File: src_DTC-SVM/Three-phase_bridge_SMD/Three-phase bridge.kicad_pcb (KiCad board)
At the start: 2 copper layers, 419.1 x 318 mm, 92 parts, among them M1 MCP6022-I/P, M2 MCP6022-I/P, P1 CONN_1, P2 POWER_FUSE, P3 CONN_2, P4 CONN_1, P5 CONN_1, P6 POWER_FUSE

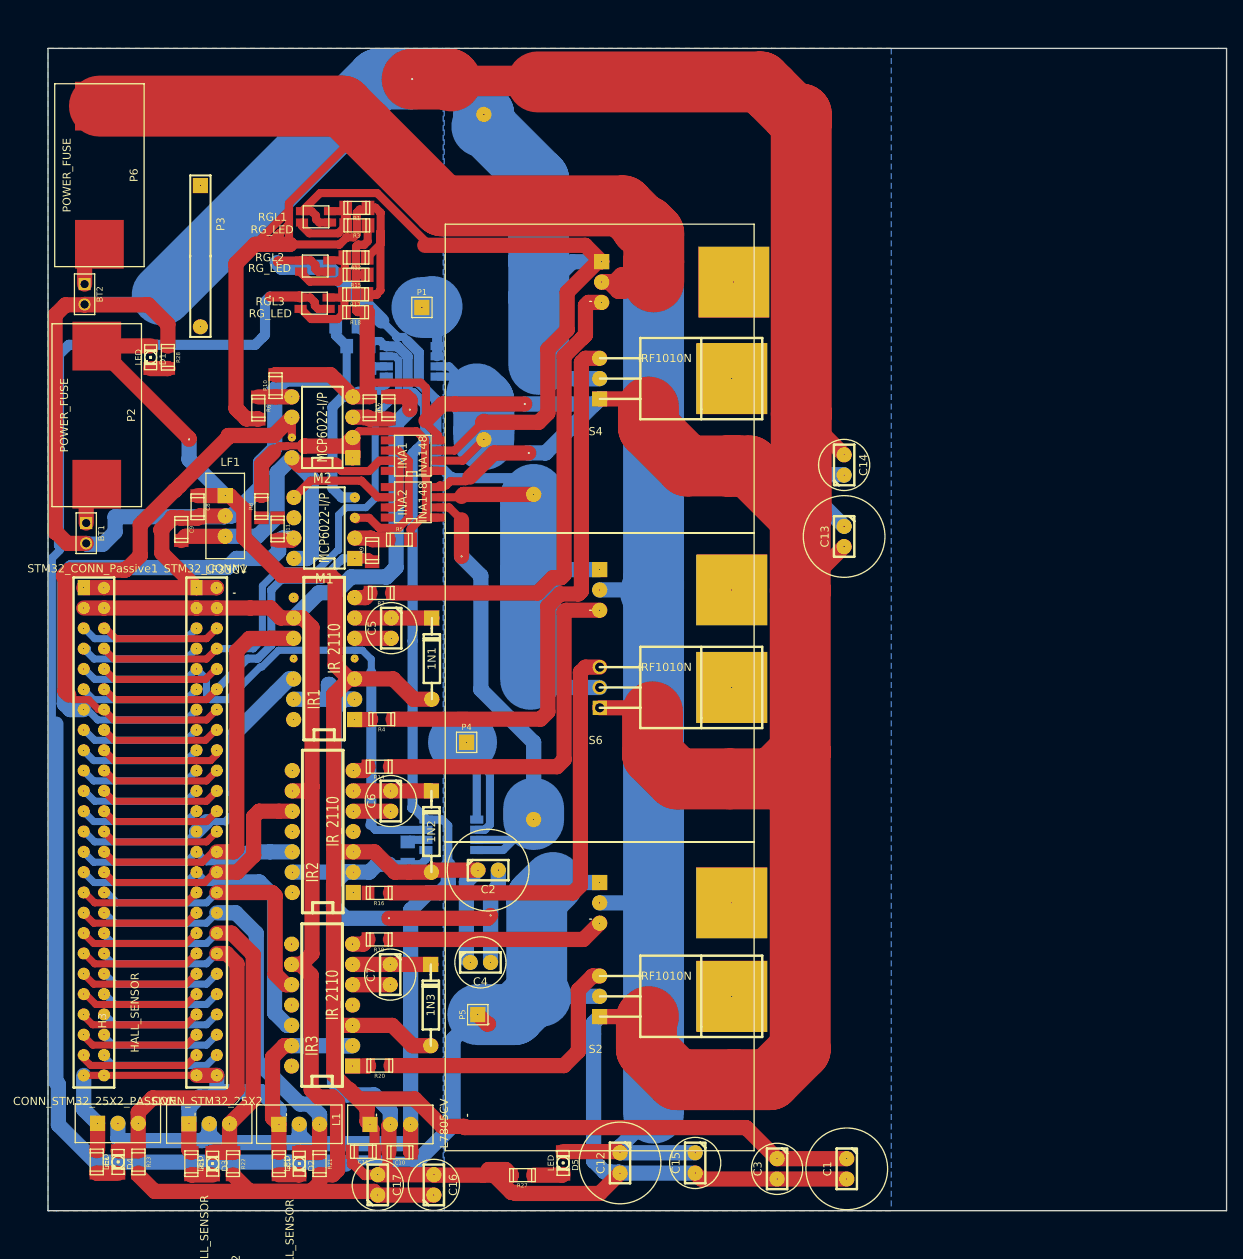
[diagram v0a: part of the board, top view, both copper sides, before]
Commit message: The fillzones for GND and 48V where added.
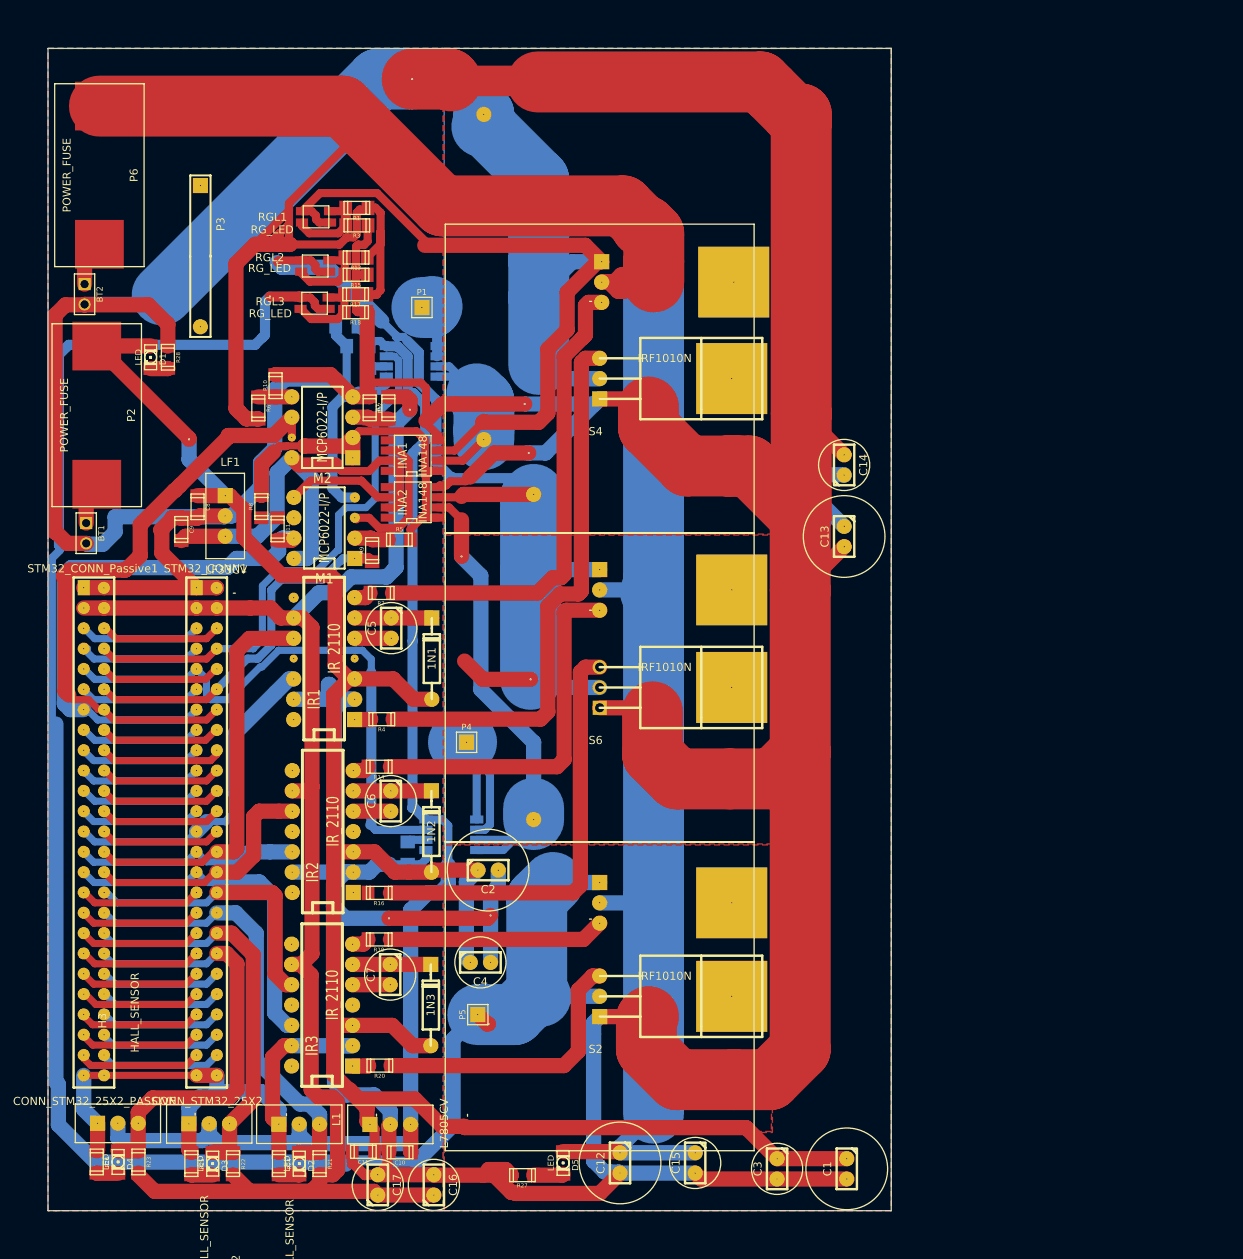
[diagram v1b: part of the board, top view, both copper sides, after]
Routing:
- net N-0000029: track 119.3 -> 128.5 mm, vias 1 -> 2
- added copper zone on F.Cu, net GND
- added copper zone on F.Cu, net N-0000012
- added copper zone on F.Cu, net N-0000029
- added copper zone on F.Cu, net N-000004
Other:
- board size 419.1 x 318 mm -> 377.2 x 318 mm
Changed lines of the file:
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@@
   (general
     (links 262)
-    (no_connects 12)
+    (no_connects 5)
     (area -125.780001 -108.254001 293.420001 219.695888)
     (thickness 1.6)
-    (drawings 8)
-    (tracks 1212)
+    (drawings 7)
+    (tracks 1215)
     (zones 0)
     (modules 92)
@@
   )
   (setup
-    (last_trace_width 0.889)
+    (last_trace_width 1.905)
     (user_trace_width 0.381)
     (user_trace_width 0.508)
@@
   )
   (gr_line (start 147.066 209.804) (end 146.05 209.804) (angle 90) (layer Edge.Cuts) (width 0.1))
-  (gr_line (start 293.37 64.516) (end 293.37 209.804) (angle 90) (layer Edge.Cuts) (width 0.1))
-  (gr_line (start 292.354 64.516) (end 293.37 64.516) (angle 90) (layer Edge.Cuts) (width 0.1))
-  (gr_line (start 236.474 64.516) (end 292.354 64.516) (angle 90) (layer Edge.Cuts) (width 0.1))
-  (gr_line (start 147.066 209.804) (end 293.37 209.804) (angle 90) (layer Edge.Cuts) (width 0.1))
+  (gr_line (start 251.46 64.516) (end 251.46 209.804) (angle 90) (layer Edge.Cuts) (width 0.1))
+  (gr_line (start 236.474 64.516) (end 251.46 64.516) (angle 90) (layer Edge.Cuts) (width 0.1))
+  (gr_line (start 147.066 209.804) (end 251.46 209.804) (angle 90) (layer Edge.Cuts) (width 0.1))
   (gr_line (start 146.05 64.516) (end 146.05 209.804) (angle 90) (layer Edge.Cuts) (width 0.1))
   (gr_line (start 236.474 64.516) (end 146.05 64.516) (angle 90) (layer Edge.Cuts) (width 0.1))
@@
   (segment (start 202.946 164.719) (end 206.756 160.909) (width 1.016) (layer B.Cu) (net 28))
   (segment (start 206.756 160.909) (end 206.756 159.512) (width 7.62) (layer B.Cu) (net 28))
+  (via (at 206.375 143.383) (size 0.254) (layers F.Cu B.Cu) (net 29))
+  (segment (start 198.12 141.097) (end 200.406 143.383) (width 1.905) (layer F.Cu) (net 29))
+  (segment (start 200.406 143.383) (end 206.375 143.383) (width 1.905) (layer F.Cu) (net 29))
   (segment (start 187.7695 98.5901) (end 181.0512 91.8718) (width 1.905) (layer B.Cu) (net 29))
   (segment (start 181.0512 91.8718) (end 175.2854 91.8718) (width 1.905) (layer B.Cu) (net 29))
@@
   (segment (start 165.989 145.415) (end 165.989 145.542) (width 0.889) (layer B.Cu) (net 50))
   (segment (start 165.989 145.542) (end 166.243 145.796) (width 0.889) (layer B.Cu) (net 50))
-  (segment (start 164.6141 142.0865) (end 165.862 143.3344) (width 0.889) (layer B.Cu) (net 50) (status 400000))
+  (segment (start 164.6141 142.0865) (end 165.862 143.3344) (width 0.889) (layer B.Cu) (net 50))
   (segment (start 166.37 145.923) (end 168.4782 145.923) (width 0.889) (layer B.Cu) (net 50))
   (segment (start 168.4782 145.923) (end 168.529 145.923) (width 0.889) (layer B.Cu) (net 50))
@@
     (connect_pads (clearance 0.0762))
     (min_thickness 0.0254)
+    (fill (arc_segments 32) (thermal_gap 0.0762) (thermal_bridge_width 1.778))
+    (polygon
+      (pts
+        (xy 195.453 209.804) (xy 146.05 209.804) (xy 146.05 64.516) (xy 195.453 64.516)
+      )
+    )
+  )
+  (zone (net 13) (net_name N-0000012) (layer F.Cu) (hatch edge 0.508)
+    (connect_pads (clearance 0.0762))
+    (min_thickness 0.0254)
+    (fill (arc_segments 32) (thermal_gap 0.0762) (thermal_bridge_width 1.778))
+    (polygon
+      (pts
+        (xy 195.58 70.231) (xy 236.728 70.231) (xy 236.728 125.222) (xy 195.707 125.222) (xy 195.58 70.231)
+      )
+    )
+  )
+  (zone (net 29) (net_name N-0000029) (layer F.Cu) (hatch edge 0.508)
+    (connect_pads (clearance 0.0762))
+    (min_thickness 0.0254)
+    (fill (arc_segments 32) (thermal_gap 0.0762) (thermal_bridge_width 1.778))
+    (polygon
+      (pts
+        (xy 236.601 163.957) (xy 195.707 163.957) (xy 195.707 125.349) (xy 236.601 125.349)
+      )
+    )
+  )
+  (zone (net 41) (net_name N-000004) (layer F.Cu) (hatch edge 0.508)
+    (connect_pads (clearance 0.0762))
+    (min_thickness 0.0254)
+    (fill (arc_segments 32) (thermal_gap 0.0762) (thermal_bridge_width 1.778))
+    (polygon
+      (pts
+        (xy 236.601 164.084) (xy 236.474 199.898) (xy 195.707 199.898) (xy 195.707 164.084)
+      )
+    )
+  )
+  (zone (net 4) (net_name GND) (layer F.Cu) (hatch edge 0.508)
+    (connect_pads (clearance 0.0762))
+    (min_thickness 0.0254)
+    (fill (arc_segments 32) (thermal_gap 0.0762) (thermal_bridge_width 1.778))
+    (polygon
+      (pts
+        (xy 251.46 209.804) (xy 195.58 209.804) (xy 195.58 200.025) (xy 236.601 200.025) (xy 236.601 196.977)
+        (xy 236.982 196.977) (xy 236.982 69.215) (xy 195.58 69.215) (xy 195.58 64.516) (xy 251.46 64.516)
+      )
+    )
+  )
+  (zone (net 4) (net_name GND) (layer F.Cu) (hatch edge 0.508)
+    (connect_pads (clearance 0.0762))
+    (min_thickness 0.0254)
